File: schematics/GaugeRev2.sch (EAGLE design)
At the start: 37 parts, among them U1 ARDUINO_MINI, U2 VID29, U3 FT232RL-BASICSSOP

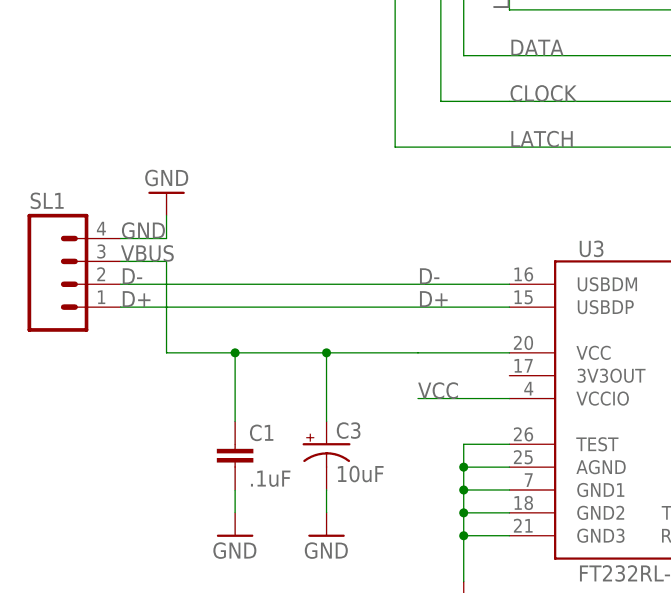
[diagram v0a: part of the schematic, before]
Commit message: layout completed for V3
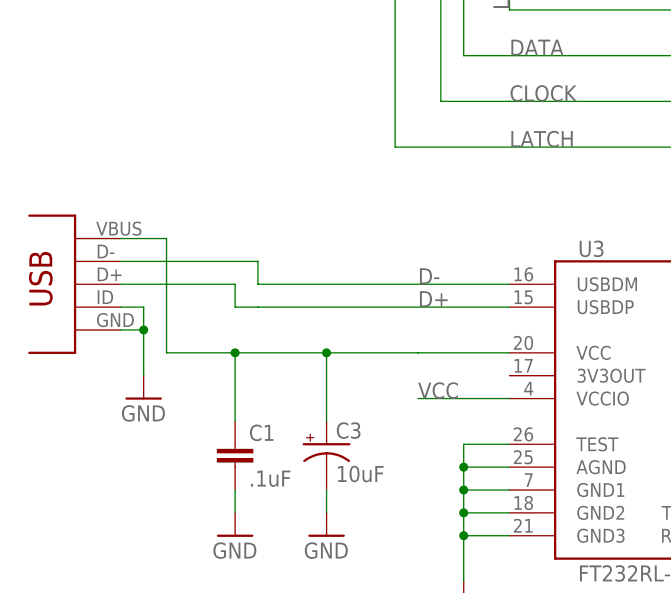
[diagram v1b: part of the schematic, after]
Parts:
- removed SL1: (no value), con-amp-quick:M04
- added U$1: USB-MINI-VERT, Evans:USB-MINI-VERT
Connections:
- net D+: now also U$1.D+; no longer SL1.1
- net D-: now also U$1.D-; no longer SL1.2
- net GND: now also U$1.GND, U$1.ID; no longer SL1.4
- net VBUS: now also U$1.VBUS; no longer SL1.3
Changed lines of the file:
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@@
 <part name="GND7" library="SparkFun" deviceset="GND" device=""/>
 <part name="GND8" library="SparkFun" deviceset="GND" device=""/>
-<part name="SL1" library="con-amp-quick" deviceset="M04" device=""/>
 <part name="GND9" library="SparkFun" deviceset="GND" device=""/>
+<part name="U$1" library="Evans" deviceset="USB-MINI-VERT" device=""/>
 </parts>
 <sheets>
@@
 <instance part="GND7" gate="1" x="35.56" y="17.78"/>
 <instance part="GND8" gate="1" x="45.72" y="17.78"/>
-<instance part="SL1" gate="G$1" x="17.78" y="45.72"/>
-<instance part="GND9" gate="1" x="27.94" y="55.88" rot="R180"/>
+<instance part="GND9" gate="1" x="25.4" y="33.02"/>
+<instance part="U$1" gate="G$1" x="17.78" y="45.72"/>
 </instances>
 <busses>
@@
 </segment>
 <segment>
-<pinref part="SL1" gate="G$1" pin="4"/>
-<wire x1="22.86" y1="50.8" x2="27.94" y2="50.8" width="0.1524" layer="91"/>
-<wire x1="27.94" y1="50.8" x2="27.94" y2="53.34" width="0.1524" layer="91"/>
+<wire x1="22.86" y1="40.64" x2="25.4" y2="40.64" width="0.1524" layer="91"/>
+<wire x1="25.4" y1="40.64" x2="25.4" y2="35.56" width="0.1524" layer="91"/>
 <pinref part="GND9" gate="1" pin="GND"/>
-<label x="22.86" y="50.8" size="1.778" layer="95"/>
+<pinref part="U$1" gate="G$1" pin="GND"/>
+<pinref part="U$1" gate="G$1" pin="ID"/>
+<wire x1="22.86" y1="43.18" x2="25.4" y2="43.18" width="0.1524" layer="91"/>
+<wire x1="25.4" y1="43.18" x2="25.4" y2="40.64" width="0.1524" layer="91"/>
+<junction x="25.4" y="40.64"/>
 </segment>
 <segment>
@@
 <segment>
 <pinref part="U3" gate="G$1" pin="USBDM"/>
-<wire x1="66.04" y1="45.72" x2="22.86" y2="45.72" width="0.1524" layer="91"/>
+<wire x1="66.04" y1="45.72" x2="38.1" y2="45.72" width="0.1524" layer="91"/>
 <label x="55.88" y="45.72" size="1.778" layer="95"/>
-<label x="22.86" y="45.72" size="1.778" layer="95"/>
-<pinref part="SL1" gate="G$1" pin="2"/>
+<wire x1="38.1" y1="45.72" x2="38.1" y2="48.26" width="0.1524" layer="91"/>
+<wire x1="38.1" y1="48.26" x2="22.86" y2="48.26" width="0.1524" layer="91"/>
+<pinref part="U$1" gate="G$1" pin="D-"/>
 </segment>
 </net>
@@
 <segment>
 <pinref part="U3" gate="G$1" pin="USBDP"/>
-<wire x1="66.04" y1="43.18" x2="22.86" y2="43.18" width="0.1524" layer="91"/>
+<wire x1="66.04" y1="43.18" x2="38.1" y2="43.18" width="0.1524" layer="91"/>
 <label x="55.88" y="43.18" size="1.778" layer="95"/>
-<label x="22.86" y="43.18" size="1.778" layer="95"/>
-<pinref part="SL1" gate="G$1" pin="1"/>
+<wire x1="38.1" y1="43.18" x2="35.56" y2="43.18" width="0.1524" layer="91"/>
+<wire x1="35.56" y1="43.18" x2="35.56" y2="45.72" width="0.1524" layer="91"/>
+<wire x1="35.56" y1="45.72" x2="22.86" y2="45.72" width="0.1524" layer="91"/>
+<pinref part="U$1" gate="G$1" pin="D+"/>
 </segment>
 </net>
@@
 <wire x1="45.72" y1="38.1" x2="45.72" y2="30.48" width="0.1524" layer="91"/>
 <junction x="45.72" y="38.1"/>
-<label x="22.86" y="48.26" size="1.778" layer="95"/>
-<wire x1="27.94" y1="38.1" x2="27.94" y2="48.26" width="0.1524" layer="91"/>
-<pinref part="SL1" gate="G$1" pin="3"/>
-<wire x1="27.94" y1="48.26" x2="22.86" y2="48.26" width="0.1524" layer="91"/>
-</segment>
-</net>
+<wire x1="27.94" y1="38.1" x2="27.94" y2="50.8" width="0.1524" layer="91"/>
+<wire x1="27.94" y1="50.8" x2="22.86" y2="50.8" width="0.1524" layer="91"/>
+<pinref part="U$1" gate="G$1" pin="VBUS"/>
+</segment>
+</net>
